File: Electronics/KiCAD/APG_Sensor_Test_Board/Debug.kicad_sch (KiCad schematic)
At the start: 14 parts, among them SW3 SW_SPST, SW4 SW_SPST

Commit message: new tvs diode debug changes
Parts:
- added Q1: RE1C002UNTCL, Package_TO_SOT_SMD:SOT-416, symbol Device:Q_NMOS_GSD
- added R32: 10k, Resistor_SMD:R_0603_1608Metric, symbol Device:R
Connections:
- net +3.3V: now also D1.2 (A), D2.2 (A), D3.2 (A), R21.1
- net Buzzer: now also Q1.1 (G), R32.2; no longer R21.1
- net GND: now also Q1.2 (S), R32.1; no longer BZ1.2 (-), D1.1 (K), D2.1 (K), D3.1 (K)
- net at R24.2: now also D3.1 (K); no longer D3.2 (A)
- net at R23.2: now also D2.1 (K); no longer D2.2 (A)
- net at R22.2: now also D1.1 (K); no longer D1.2 (A)
- new net: BZ1.2 (-), Q1.3 (D)
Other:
- moved on the sheet: D1, D2, D3, R22, R23, R24

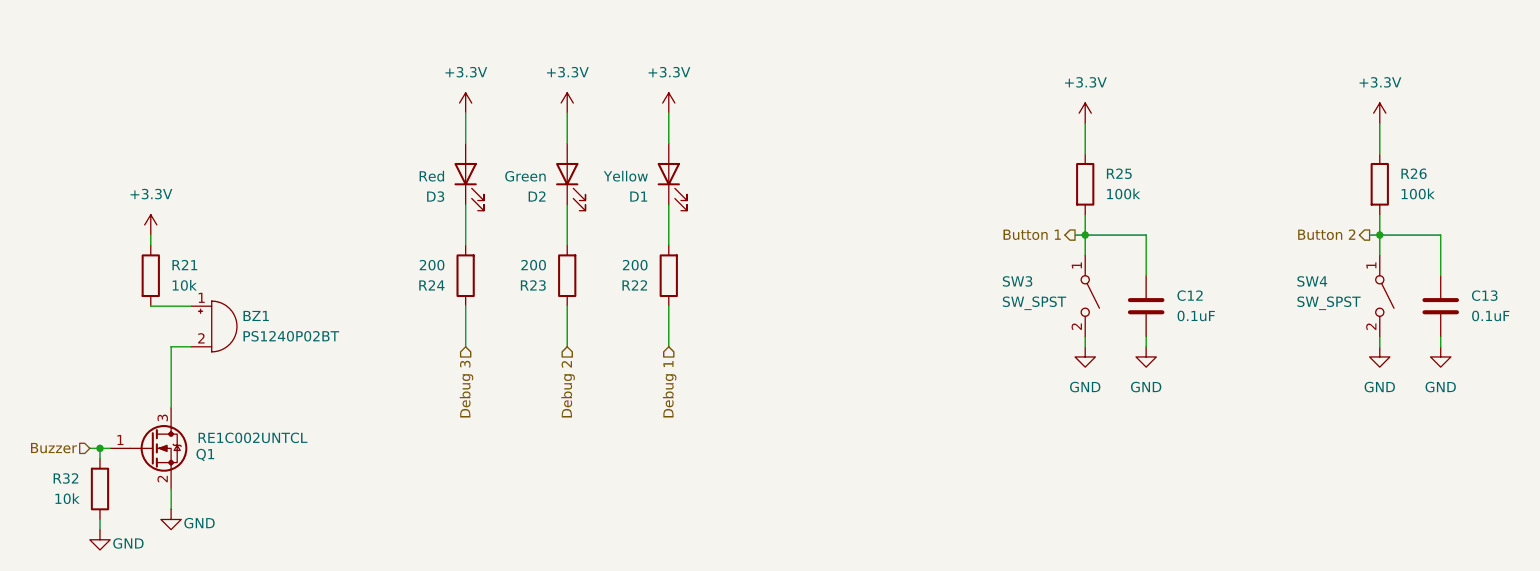
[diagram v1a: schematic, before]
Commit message: Edit PCB and Update component values
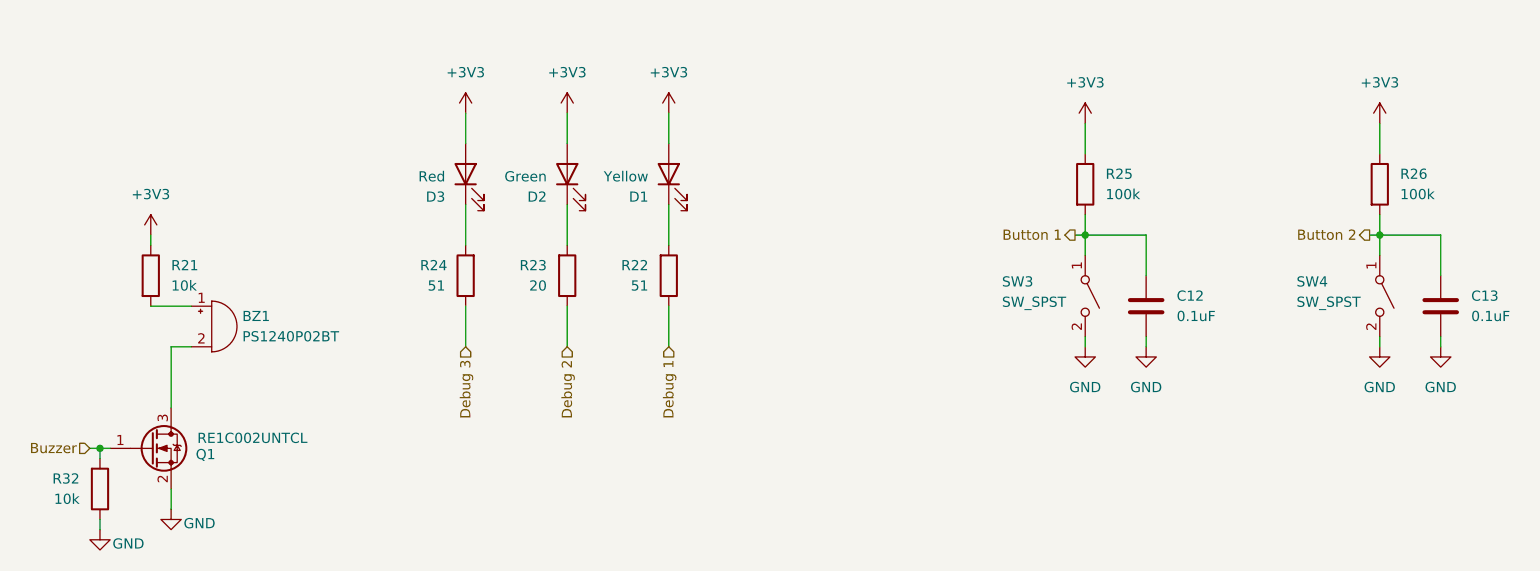
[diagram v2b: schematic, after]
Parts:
- Q1: JLCPCB (none) -> C509959
- R22, R24: value 200 -> 51
- R23: value 200 -> 20
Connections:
- net +3.3V renamed +3V3
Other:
- moved on the sheet: R22, R23
